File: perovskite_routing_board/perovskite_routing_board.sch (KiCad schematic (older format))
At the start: 7 parts, among them J1 Conn_01x08, J2 Conn_01x08, J3 Conn_01x08, J4 Conn_01x08, J5 Conn_01x08, J6 Conn_01x08, J7 G125-MH12605M4R

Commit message: routing board done and nice and pretty
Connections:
- net CELL3 is gone; now on net CELL_3: J2.4 (Pin_4)
- net ALERT1: now also J7.10
- net ALERT2: now also J7.25
- net ALERT3: now also J7.7
- net CELL_1: now also J7.9
- net CELL_10: now also J7.22
- net CELL_11: now also J7.21
- net CELL_12: now also J7.20
- net CELL_13: now also J7.18
- net CELL_14: now also J7.8
- net CELL_15: now also J7.6
- net CELL_16: now also J7.5
- net CELL_17: now also J7.16
- net CELL_18: now also J7.17
- net CELL_2: now also J7.11
- net CELL_4: now also J7.4
- net CELL_5: now also J7.3
- net CELL_6: now also J7.2
- net CELL_7: now also J7.13
- net CELL_8: now also J7.26
- net CELL_9: now also J7.24
- net CP: now also J7.1
- net GND: now also J7.19
- net SCL: now also J7.23
- net SDA: now also J7.15
- net VDD: now also J7.14
- net CELL_3: now reaches J7.12
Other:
- moved on the sheet: J7
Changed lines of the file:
@@
 L G125-MH12605M4R:G125-MH12605M4R J7
 U 1 1 636882D7
-P 6700 3125
-F 0 "J7" H 7150 3390 50  0000 C CNN
-F 1 "G125-MH12605M4R" H 7150 3299 50  0000 C CNN
-F 2 "MV12605M1P:G125-MV12605M1P" H 7450 3225 50  0001 L CNN
-F 3 "https://cdn.harwin.com/pdfs/G125-MH1XX05M4R.pdf" H 7450 3125 50  0001 L CNN
-F 4 "Gecko Screw-Lok DIL Male Horizontal Throughboard Connector, internally threaded screw fixings with board mount capability, gold, pick &amp; place (Tape &amp; Reel packing), 26 contacts" H 7450 3025 50  0001 L CNN "Description"
-F 5 "5.3" H 7450 2925 50  0001 L CNN "Height"
-F 6 "Harwin" H 7450 2825 50  0001 L CNN "Manufacturer_Name"
-F 7 "G125-MH12605M4R" H 7450 2725 50  0001 L CNN "Manufacturer_Part_Number"
-F 8 "855-G125MH1265M4RM4R" H 7450 2625 50  0001 L CNN "Mouser Part Number"
-F 9 "https://www.mouser.co.uk/ProductDetail/Harwin/G125-MH12605M4R?qs=vHuUswq2%252BsyH7SZgyn76GA%3D%3D" H 7450 2525 50  0001 L CNN "Mouser Price/Stock"
-F 10 "" H 7450 2425 50  0001 L CNN "Arrow Part Number"
-F 11 "" H 7450 2325 50  0001 L CNN "Arrow Price/Stock"
-F 12 "" H 7450 2225 50  0001 L CNN "Mouser Testing Part Number"
-F 13 "" H 7450 2125 50  0001 L CNN "Mouser Testing Price/Stock"
-	1    6700 3125
+P 6800 3150
+F 0 "J7" H 7250 3415 50  0000 C CNN
+F 1 "G125-MH12605M4R" H 7250 3324 50  0000 C CNN
+F 2 "MV12605M1P:G125-MV12605M1P" H 7550 3250 50  0001 L CNN
+F 3 "https://cdn.harwin.com/pdfs/G125-MH1XX05M4R.pdf" H 7550 3150 50  0001 L CNN
+F 4 "Gecko Screw-Lok DIL Male Horizontal Throughboard Connector, internally threaded screw fixings with board mount capability, gold, pick &amp; place (Tape &amp; Reel packing), 26 contacts" H 7550 3050 50  0001 L CNN "Description"
+F 5 "5.3" H 7550 2950 50  0001 L CNN "Height"
+F 6 "Harwin" H 7550 2850 50  0001 L CNN "Manufacturer_Name"
+F 7 "G125-MH12605M4R" H 7550 2750 50  0001 L CNN "Manufacturer_Part_Number"
+F 8 "855-G125MH1265M4RM4R" H 7550 2650 50  0001 L CNN "Mouser Part Number"
+F 9 "https://www.mouser.co.uk/ProductDetail/Harwin/G125-MH12605M4R?qs=vHuUswq2%252BsyH7SZgyn76GA%3D%3D" H 7550 2550 50  0001 L CNN "Mouser Price/Stock"
+F 10 "" H 7550 2450 50  0001 L CNN "Arrow Part Number"
+F 11 "" H 7550 2350 50  0001 L CNN "Arrow Price/Stock"
+F 12 "" H 7550 2250 50  0001 L CNN "Mouser Testing Part Number"
+F 13 "" H 7550 2150 50  0001 L CNN "Mouser Testing Price/Stock"
+	1    6800 3150
 	1    0    0    -1
 $EndComp
@@
 ALERT1
 Text GLabel 2650 2750 1    50   Input ~ 0
-CELL3
+CELL_3
 Wire Wire Line
 	1950 2350 2050 2350
@@
 	-1   0    0    1
 $EndComp
+Text GLabel 7700 4350 2    50   Input ~ 0
+CP
+Text GLabel 7700 4150 2    50   Input ~ 0
+CELL_5
+Text GLabel 7700 4250 2    50   Input ~ 0
+CELL_6
+Text GLabel 6800 3750 0    50   Input ~ 0
+CELL_12
+Text GLabel 6800 3650 0    50   Input ~ 0
+CELL_11
+Text GLabel 6800 3550 0    50   Input ~ 0
+CELL_10
+Text GLabel 6800 3450 0    50   Input ~ 0
+SCL
+Text GLabel 6800 4050 0    50   Input ~ 0
+CELL_18
+Text GLabel 6800 4150 0    50   Input ~ 0
+CELL_17
+Text GLabel 6800 4250 0    50   Input ~ 0
+SDA
+Text GLabel 7700 3950 2    50   Input ~ 0
+CELL_16
+Text GLabel 6800 3950 0    50   Input ~ 0
+CELL_13
+Text GLabel 7700 3750 2    50   Input ~ 0
+ALERT3
+Text GLabel 7700 3850 2    50   Input ~ 0
+CELL_15
+Text GLabel 7700 4050 2    50   Input ~ 0
+CELL_4
+Text GLabel 7700 3350 2    50   Input ~ 0
+CELL_2
+Text GLabel 6800 3350 0    50   Input ~ 0
+CELL_9
+Text GLabel 6800 3250 0    50   Input ~ 0
+ALERT2
+Text GLabel 7700 3150 2    50   Input ~ 0
+CELL_7
+Text GLabel 7700 3250 2    50   Input ~ 0
+CELL_3
+Text GLabel 7700 3450 2    50   Input ~ 0
+ALERT1
+Text GLabel 7700 3550 2    50   Input ~ 0
+CELL_1
+$Comp
+L power:VDD #PWR0120
+U 1 1 638E12AD
+P 6800 4350
+F 0 "#PWR0120" H 6800 4200 50  0001 C CNN
+F 1 "VDD" V 6815 4477 50  0000 L CNN
+F 2 "" H 6800 4350 50  0001 C CNN
+F 3 "" H 6800 4350 50  0001 C CNN
+	1    6800 4350
+	0    -1   -1   0
+$EndComp
+Text GLabel 6800 3150 0    50   Input ~ 0
+CELL_8
+Text GLabel 7700 3650 2    50   Input ~ 0
+CELL_14
+$Comp
+L power:GND #PWR?
+U 1 1 63968B87
+P 6800 3850
+F 0 "#PWR?" H 6800 3600 50  0001 C CNN
+F 1 "GND" V 6805 3722 50  0000 R CNN
+F 2 "" H 6800 3850 50  0001 C CNN
+F 3 "" H 6800 3850 50  0001 C CNN
+	1    6800 3850
+	0    1    1    0
+$EndComp
 $EndSCHEMATC

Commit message: added pull up resistor
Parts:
- added R1, R2: R, Resistor_SMD:R_0603_1608Metric, symbol Device:R
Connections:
- net SCL: now also R1.2
- net SDA: now also R2.2
- net VDD: now also R1.1, R2.1
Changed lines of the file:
@@
 CELL_14
 $Comp
-L power:GND #PWR?
+L power:GND #PWR0119
 U 1 1 63968B87
 P 6800 3850
-F 0 "#PWR?" H 6800 3600 50  0001 C CNN
+F 0 "#PWR0119" H 6800 3600 50  0001 C CNN
 F 1 "GND" V 6805 3722 50  0000 R CNN
 F 2 "" H 6800 3850 50  0001 C CNN
@@
 	0    1    1    0
 $EndComp
+$Comp
+L Device:R R1
+U 1 1 6396BC94
+P 5000 3950
+F 0 "R1" H 5070 3996 50  0000 L CNN
+F 1 "R" H 5070 3905 50  0000 L CNN
+F 2 "Resistor_SMD:R_0603_1608Metric" V 4930 3950 50  0001 C CNN
+F 3 "~" H 5000 3950 50  0001 C CNN
+	1    5000 3950
+	1    0    0    -1
+$EndComp
+$Comp
+L Device:R R2
+U 1 1 6396BF50
+P 5300 3950
+F 0 "R2" H 5370 3996 50  0000 L CNN
+F 1 "R" H 5370 3905 50  0000 L CNN
+F 2 "Resistor_SMD:R_0603_1608Metric" V 5230 3950 50  0001 C CNN
+F 3 "~" H 5300 3950 50  0001 C CNN
+	1    5300 3950
+	1    0    0    -1
+$EndComp
+Text GLabel 5000 4100 3    50   Input ~ 0
+SCL
+Text GLabel 5300 4100 3    50   Input ~ 0
+SDA
+$Comp
+L power:VDD #PWR01
+U 1 1 6396C4FE
+P 5000 3800
+F 0 "#PWR01" H 5000 3650 50  0001 C CNN
+F 1 "VDD" H 5015 3973 50  0000 C CNN
+F 2 "" H 5000 3800 50  0001 C CNN
+F 3 "" H 5000 3800 50  0001 C CNN
+	1    5000 3800
+	1    0    0    -1
+$EndComp
+$Comp
+L power:VDD #PWR02
+U 1 1 6396CBD4
+P 5300 3800
+F 0 "#PWR02" H 5300 3650 50  0001 C CNN
+F 1 "VDD" H 5315 3973 50  0000 C CNN
+F 2 "" H 5300 3800 50  0001 C CNN
+F 3 "" H 5300 3800 50  0001 C CNN
+	1    5300 3800
+	1    0    0    -1
+$EndComp
 $EndSCHEMATC

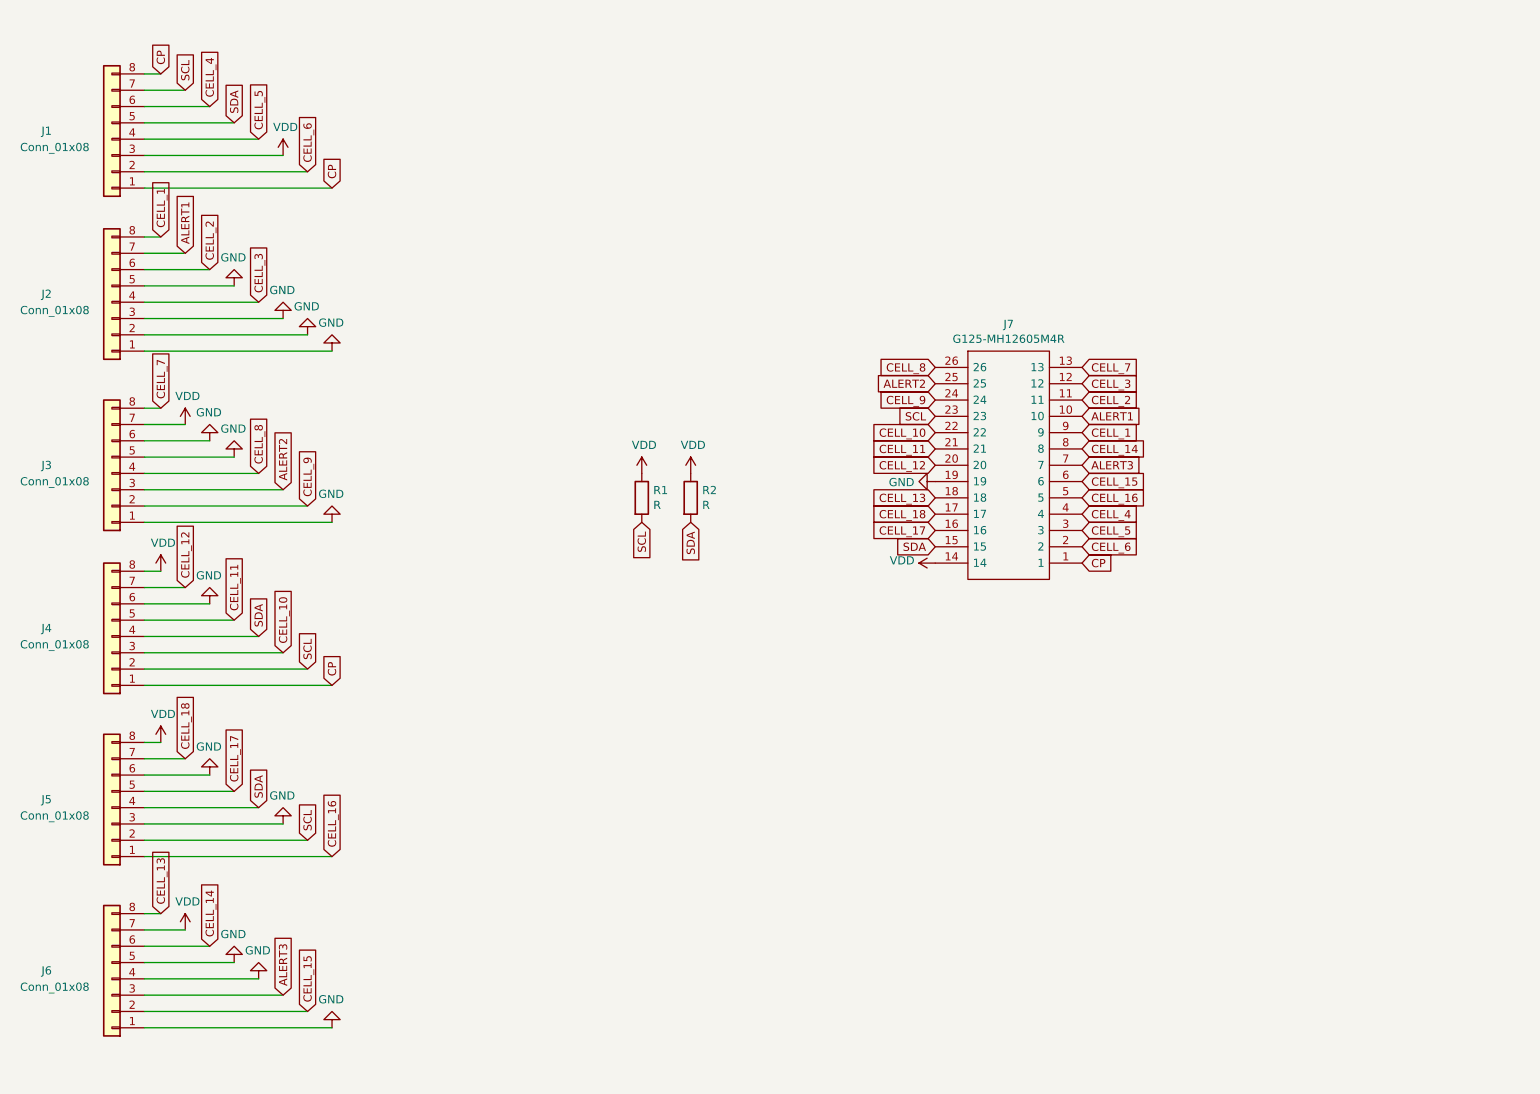
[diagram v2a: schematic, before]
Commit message: Updating designs
- Generate gerbers
- Generate renders
- Working on layout for payload controller
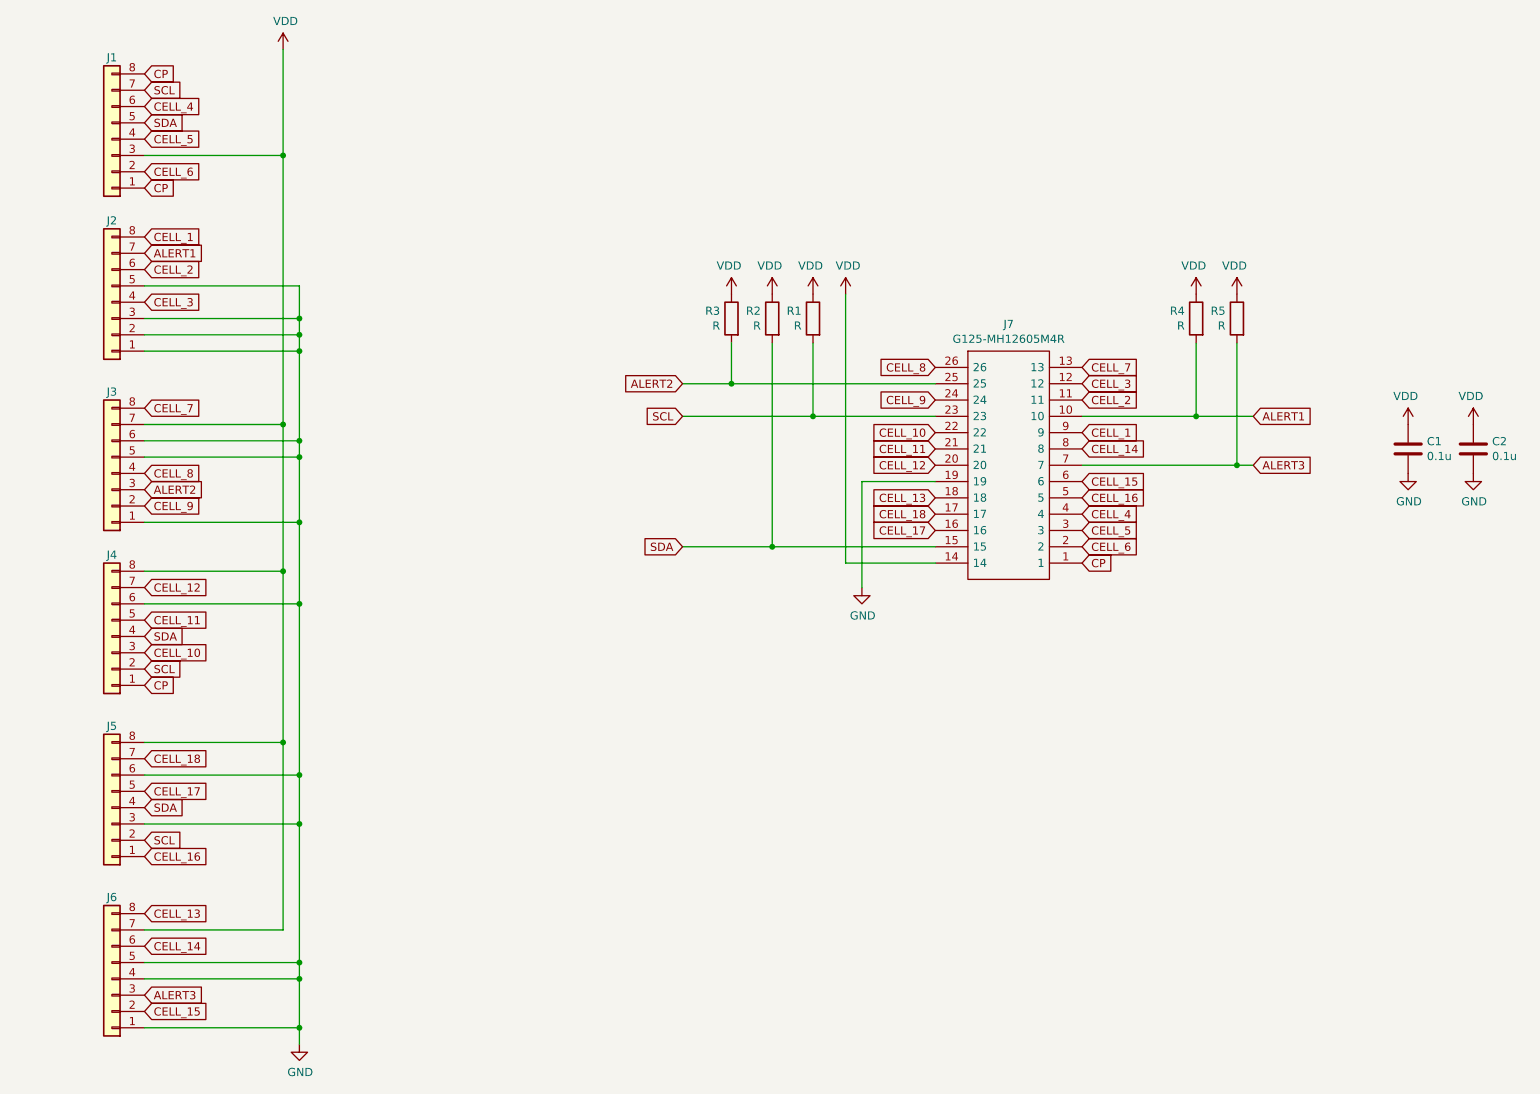
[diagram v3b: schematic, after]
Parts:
- added C1, C2: 0.1u, Capacitor_SMD:C_0603_1608Metric, symbol Device:C
- added R3, R4, R5: R, Resistor_SMD:R_0603_1608Metric, symbol Device:R
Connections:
- net ALERT1: now also R4.2
- net ALERT2: now also R3.2
- net ALERT3: now also R5.2
- net GND: now also C1.2, C2.2
- net VDD: now also C1.1, C2.1, R3.1, R4.1, R5.1
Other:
- moved on the sheet: R1, R2

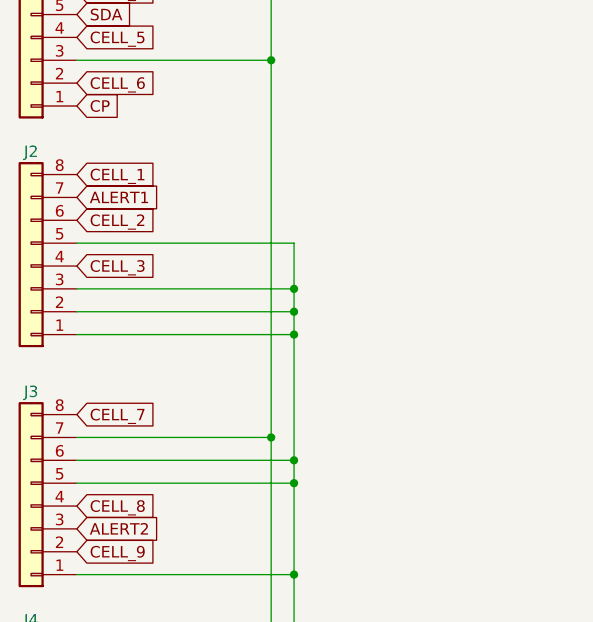
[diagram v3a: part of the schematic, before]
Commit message: fixed backwards connector on routing board
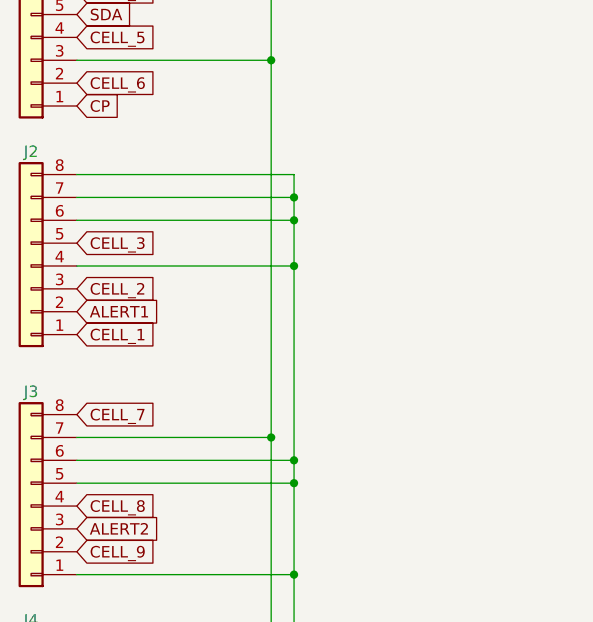
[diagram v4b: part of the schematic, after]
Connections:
- net ALERT1: now also J2.2 (Pin_2); no longer J2.7 (Pin_7)
- net CELL_1: now also J2.1 (Pin_1); no longer J2.8 (Pin_8)
- net CELL_2: now also J2.3 (Pin_3); no longer J2.6 (Pin_6)
- net CELL_3: now also J2.5 (Pin_5); no longer J2.4 (Pin_4)
- net GND: now also J2.4 (Pin_4), J2.6 (Pin_6), J2.7 (Pin_7), J2.8 (Pin_8); no longer J2.1 (Pin_1), J2.2 (Pin_2), J2.3 (Pin_3), J2.5 (Pin_5)
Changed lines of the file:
@@
 Text GLabel 1950 1450 2    50   Input ~ 0
 SCL
-Text GLabel 1950 2450 2    50   Input ~ 0
+Text GLabel 1950 2950 2    50   Input ~ 0
 ALERT1
-Text GLabel 1950 2750 2    50   Input ~ 0
+Text GLabel 1950 2650 2    50   Input ~ 0
 CELL_3
 Text GLabel 1950 3400 2    50   Input ~ 0
@@
 Text GLabel 1950 7100 2    50   Input ~ 0
 CELL_15
-Text GLabel 1950 2550 2    50   Input ~ 0
+Text GLabel 1950 2850 2    50   Input ~ 0
 CELL_2
 $Comp
@@
 Text GLabel 1950 1550 2    50   Input ~ 0
 CELL_4
-Text GLabel 1950 2350 2    50   Input ~ 0
+Text GLabel 1950 3050 2    50   Input ~ 0
 CELL_1
 Wire Wire Line
@@
 Wire Wire Line
 	2800 1850 2800 1200
-Wire Wire Line
-	2800 3500 2800 1850
 Connection ~ 2800 1850
 Wire Wire Line
@@
 Wire Wire Line
 	1950 3700 2900 3700
-Wire Wire Line
-	2900 3050 2900 3600
 Connection ~ 2900 3600
-Wire Wire Line
-	1950 3050 2900 3050
-Wire Wire Line
-	1950 2950 2900 2950
-Wire Wire Line
-	2900 2950 2900 3050
-Connection ~ 2900 3050
-Wire Wire Line
-	1950 2850 2900 2850
-Wire Wire Line
-	2900 2850 2900 2950
-Connection ~ 2900 2950
-Wire Wire Line
-	1950 2650 2900 2650
-Wire Wire Line
-	2900 2650 2900 2850
-Connection ~ 2900 2850
 Wire Wire Line
 	6800 3450 6050 3450
@@
 	1    0    0    -1
 $EndComp
+Wire Wire Line
+	2800 3500 2800 1850
+Wire Wire Line
+	1950 2750 2900 2750
+Connection ~ 2900 2750
+Wire Wire Line
+	2900 2750 2900 3600
+Wire Wire Line
+	1950 2350 2900 2350
+Wire Wire Line
+	1950 2450 2900 2450
+Wire Wire Line
+	2900 2350 2900 2450
+Connection ~ 2900 2450
+Wire Wire Line
+	1950 2550 2900 2550
+Wire Wire Line
+	2900 2450 2900 2550
+Connection ~ 2900 2550
+Wire Wire Line
+	2900 2550 2900 2750
 $EndSCHEMATC
